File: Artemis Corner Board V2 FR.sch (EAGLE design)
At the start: 102 parts, among them IC1 FT232RL, Q1 BSS138, U1 OPA365AIDBVR, U2 ADS1232IPWR, U3 MCP2562, U4 TM4C123GH6PMI, U5 MCP2562, U6 TPS62177, U7 TPS62175, U8 TPS562219, Y1 16MHz, Y2 32.768kHz

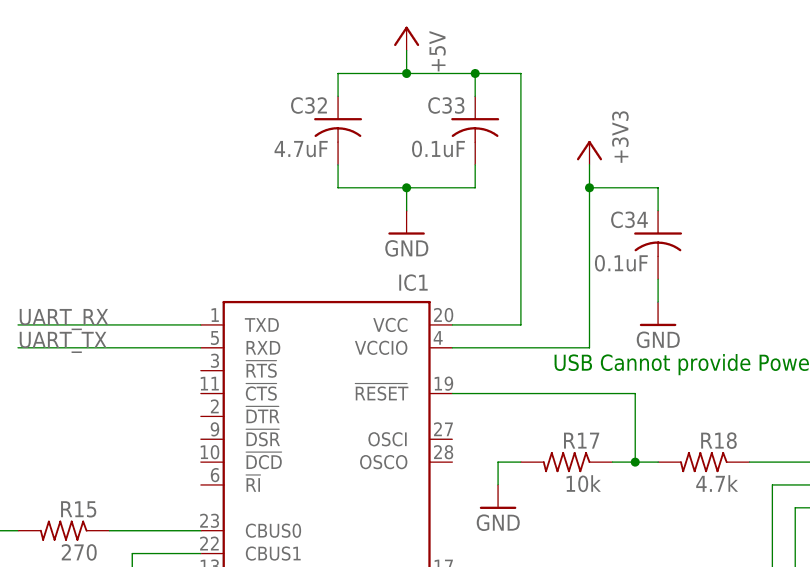
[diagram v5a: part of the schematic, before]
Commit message: Grouped components in layout
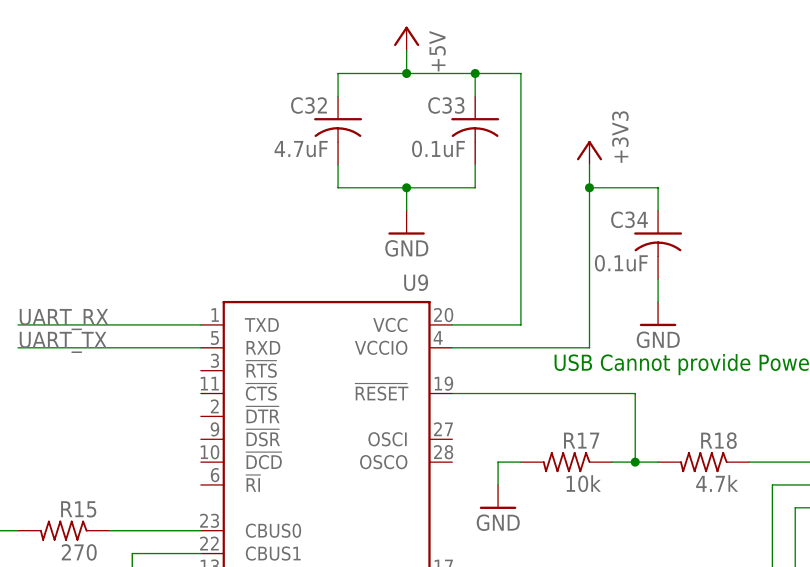
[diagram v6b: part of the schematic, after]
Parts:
- renumbered IC1 to U9
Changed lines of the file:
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@@
 <part name="+3V311" library="supply1" deviceset="+3V3" device=""/>
 <part name="+1V21" library="FormE" deviceset="+1V2" device=""/>
-<part name="IC1" library="ftdichip" deviceset="FT232R" device="L">
+<part name="U9" library="ftdichip" deviceset="FT232R" device="L">
 <attribute name="PARTNO" value="FT232RL-REEL"/>
 </part>
@@
 <instance part="+3V311" gate="G$1" x="878.84" y="185.42"/>
 <instance part="+1V21" gate="G$1" x="878.84" y="124.46"/>
-<instance part="IC1" gate="1" x="612.14" y="200.66" rot="MR0">
+<instance part="U9" gate="1" x="612.14" y="200.66" rot="MR0">
 <attribute name="PARTNO" x="612.14" y="200.66" size="1.778" layer="96" rot="MR0" display="off"/>
 </instance>
@@
 <pinref part="GND37" gate="1" pin="GND"/>
 <wire x1="594.36" y1="170.18" x2="594.36" y2="175.26" width="0.1524" layer="91"/>
-<pinref part="IC1" gate="1" pin="GND@2"/>
+<pinref part="U9" gate="1" pin="GND@2"/>
 <wire x1="594.36" y1="175.26" x2="596.9" y2="175.26" width="0.1524" layer="91"/>
 <wire x1="594.36" y1="175.26" x2="594.36" y2="177.8" width="0.1524" layer="91"/>
 <junction x="594.36" y="175.26"/>
-<pinref part="IC1" gate="1" pin="GND@1"/>
+<pinref part="U9" gate="1" pin="GND@1"/>
 <wire x1="594.36" y1="177.8" x2="596.9" y2="177.8" width="0.1524" layer="91"/>
-<pinref part="IC1" gate="1" pin="GND"/>
+<pinref part="U9" gate="1" pin="GND"/>
 <wire x1="596.9" y1="180.34" x2="594.36" y2="180.34" width="0.1524" layer="91"/>
 <wire x1="594.36" y1="180.34" x2="594.36" y2="177.8" width="0.1524" layer="91"/>
@@
 <wire x1="594.36" y1="180.34" x2="594.36" y2="185.42" width="0.1524" layer="91"/>
 <junction x="594.36" y="180.34"/>
-<pinref part="IC1" gate="1" pin="TEST"/>
+<pinref part="U9" gate="1" pin="TEST"/>
 <wire x1="594.36" y1="185.42" x2="596.9" y2="185.42" width="0.1524" layer="91"/>
 </segment>
 <segment>
 <pinref part="GND40" gate="1" pin="GND"/>
-<pinref part="IC1" gate="1" pin="GND@A"/>
+<pinref part="U9" gate="1" pin="GND@A"/>
 <wire x1="629.92" y1="165.1" x2="629.92" y2="182.88" width="0.1524" layer="91"/>
 <wire x1="629.92" y1="182.88" x2="624.84" y2="182.88" width="0.1524" layer="91"/>
@@
 <wire x1="619.76" y1="254" x2="619.76" y2="251.46" width="0.1524" layer="91"/>
 <junction x="619.76" y="251.46"/>
-<pinref part="IC1" gate="1" pin="VCC"/>
+<pinref part="U9" gate="1" pin="VCC"/>
 <wire x1="624.84" y1="223.52" x2="632.46" y2="223.52" width="0.1524" layer="91"/>
 <wire x1="632.46" y1="223.52" x2="632.46" y2="251.46" width="0.1524" layer="91"/>
@@
 <pinref part="+3V310" gate="G$1" pin="+3V3"/>
 <wire x1="640.08" y1="220.98" x2="640.08" y2="238.76" width="0.1524" layer="91"/>
-<pinref part="IC1" gate="1" pin="VCCIO"/>
+<pinref part="U9" gate="1" pin="VCCIO"/>
 <wire x1="640.08" y1="238.76" x2="640.08" y2="241.3" width="0.1524" layer="91"/>
 <wire x1="624.84" y1="220.98" x2="640.08" y2="220.98" width="0.1524" layer="91"/>
@@
 <segment>
 <label x="576.58" y="220.98" size="1.778" layer="95"/>
-<pinref part="IC1" gate="1" pin="RXD"/>
+<pinref part="U9" gate="1" pin="RXD"/>
 <wire x1="576.58" y1="220.98" x2="596.9" y2="220.98" width="0.1524" layer="91"/>
 </segment>
@@
 <net name="UART_RX" class="0">
 <segment>
-<pinref part="IC1" gate="1" pin="TXD"/>
+<pinref part="U9" gate="1" pin="TXD"/>
 <wire x1="596.9" y1="223.52" x2="576.58" y2="223.52" width="0.1524" layer="91"/>
 <label x="576.58" y="223.52" size="1.778" layer="95"/>
@@
 <wire x1="589.28" y1="198.12" x2="589.28" y2="190.5" width="0.1524" layer="91"/>
 <wire x1="589.28" y1="190.5" x2="586.74" y2="190.5" width="0.1524" layer="91"/>
-<pinref part="IC1" gate="1" pin="CBUS1"/>
+<pinref part="U9" gate="1" pin="CBUS1"/>
 <wire x1="596.9" y1="198.12" x2="589.28" y2="198.12" width="0.1524" layer="91"/>
 </segment>
@@
 <segment>
 <pinref part="R15" gate="G$1" pin="1"/>
-<pinref part="IC1" gate="1" pin="CBUS0"/>
+<pinref part="U9" gate="1" pin="CBUS0"/>
 <wire x1="586.74" y1="200.66" x2="596.9" y2="200.66" width="0.1524" layer="91"/>
 </segment>
@@
 <net name="USB_D_N" class="1">
 <segment>
-<pinref part="IC1" gate="1" pin="USBDM"/>
+<pinref part="U9" gate="1" pin="USBDM"/>
 <wire x1="624.84" y1="187.96" x2="660.4" y2="187.96" width="0.1524" layer="91"/>
 <wire x1="660.4" y1="187.96" x2="660.4" y2="205.74" width="0.1524" layer="91"/>
@@
 <wire x1="670.56" y1="203.2" x2="662.94" y2="203.2" width="0.1524" layer="91"/>
 <wire x1="662.94" y1="203.2" x2="662.94" y2="190.5" width="0.1524" layer="91"/>
-<pinref part="IC1" gate="1" pin="USBDP"/>
+<pinref part="U9" gate="1" pin="USBDP"/>
 <wire x1="662.94" y1="190.5" x2="624.84" y2="190.5" width="0.1524" layer="91"/>
 </segment>
@@
 <pinref part="C35" gate="G$1" pin="1"/>
 <wire x1="652.78" y1="182.88" x2="652.78" y2="195.58" width="0.1524" layer="91"/>
-<pinref part="IC1" gate="1" pin="3V3OUT"/>
+<pinref part="U9" gate="1" pin="3V3OUT"/>
 <wire x1="652.78" y1="195.58" x2="624.84" y2="195.58" width="0.1524" layer="91"/>
 </segment>
@@
 <wire x1="645.16" y1="208.28" x2="645.16" y2="215.9" width="0.1524" layer="91"/>
 <junction x="645.16" y="208.28"/>
-<pinref part="IC1" gate="1" pin="!RESET"/>
+<pinref part="U9" gate="1" pin="!RESET"/>
 <wire x1="645.16" y1="215.9" x2="624.84" y2="215.9" width="0.1524" layer="91"/>
 </segment>

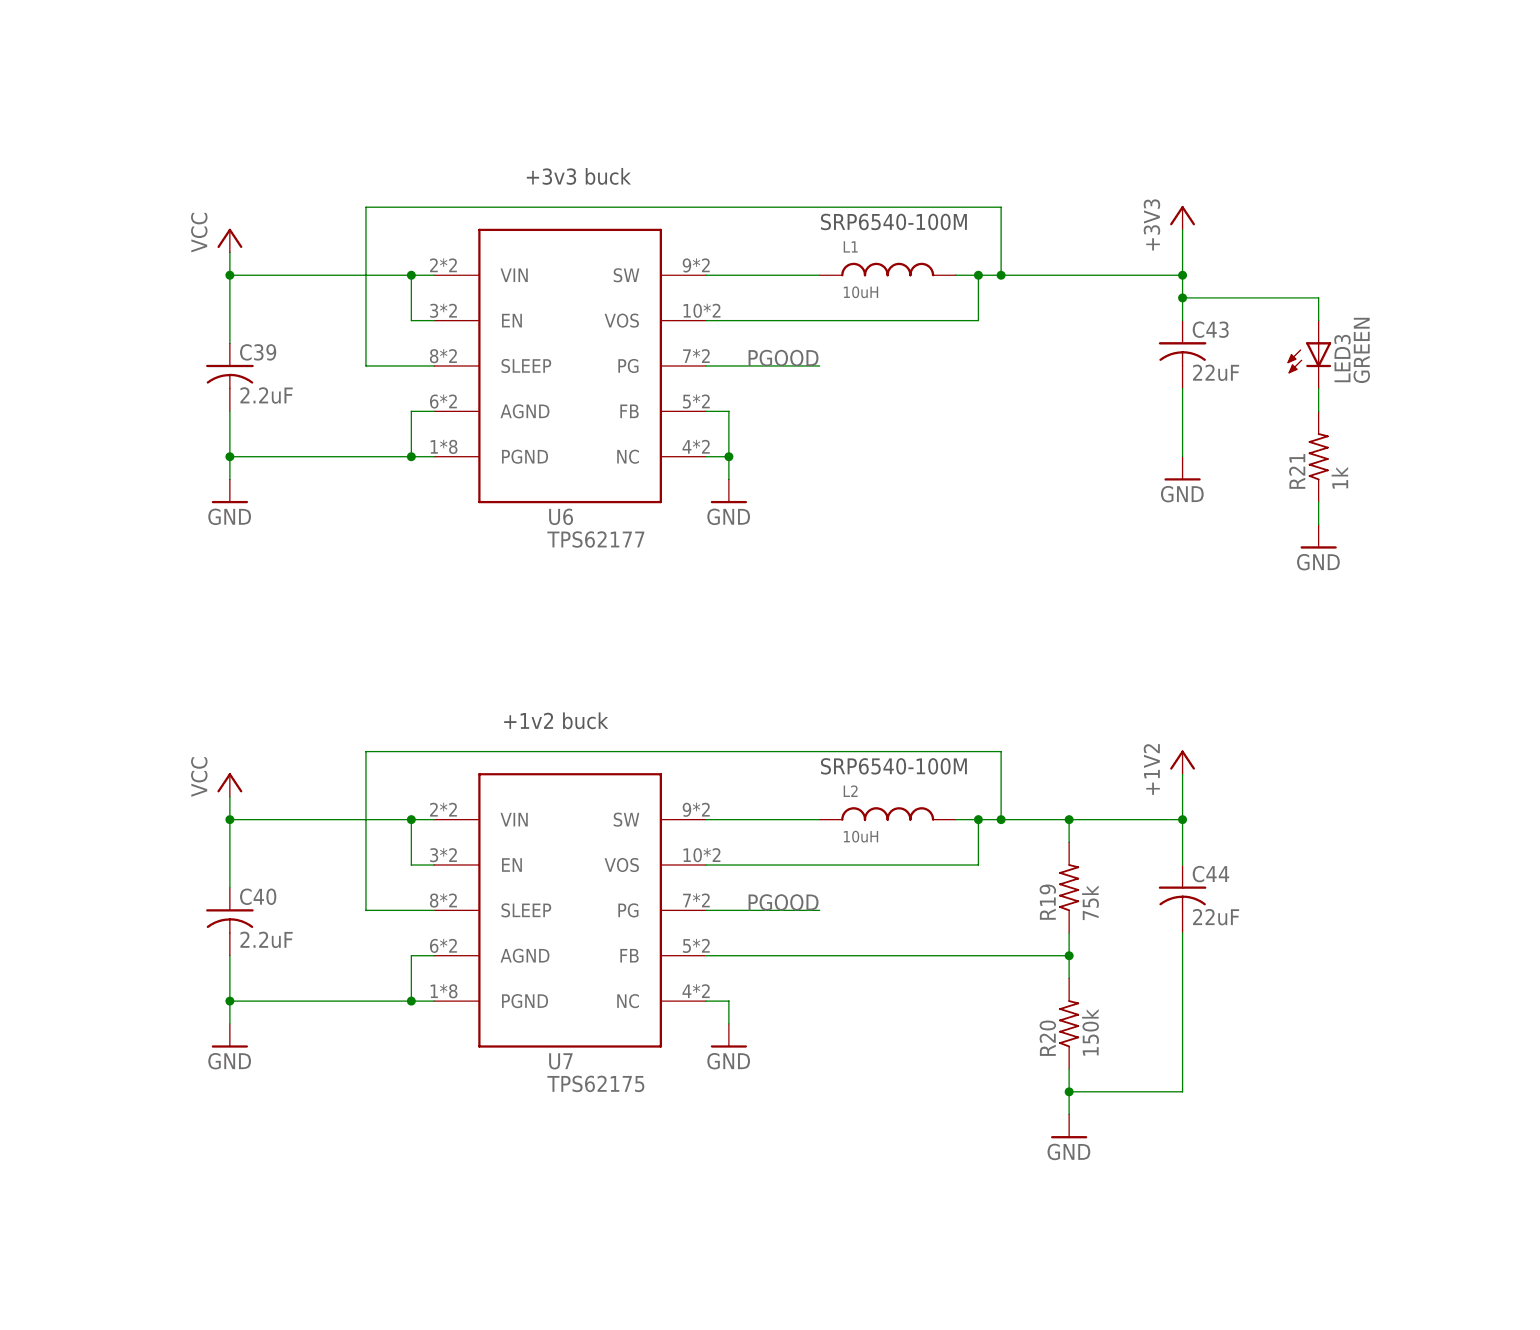
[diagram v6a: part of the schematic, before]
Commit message: Changed to smaller LM3671 regulators
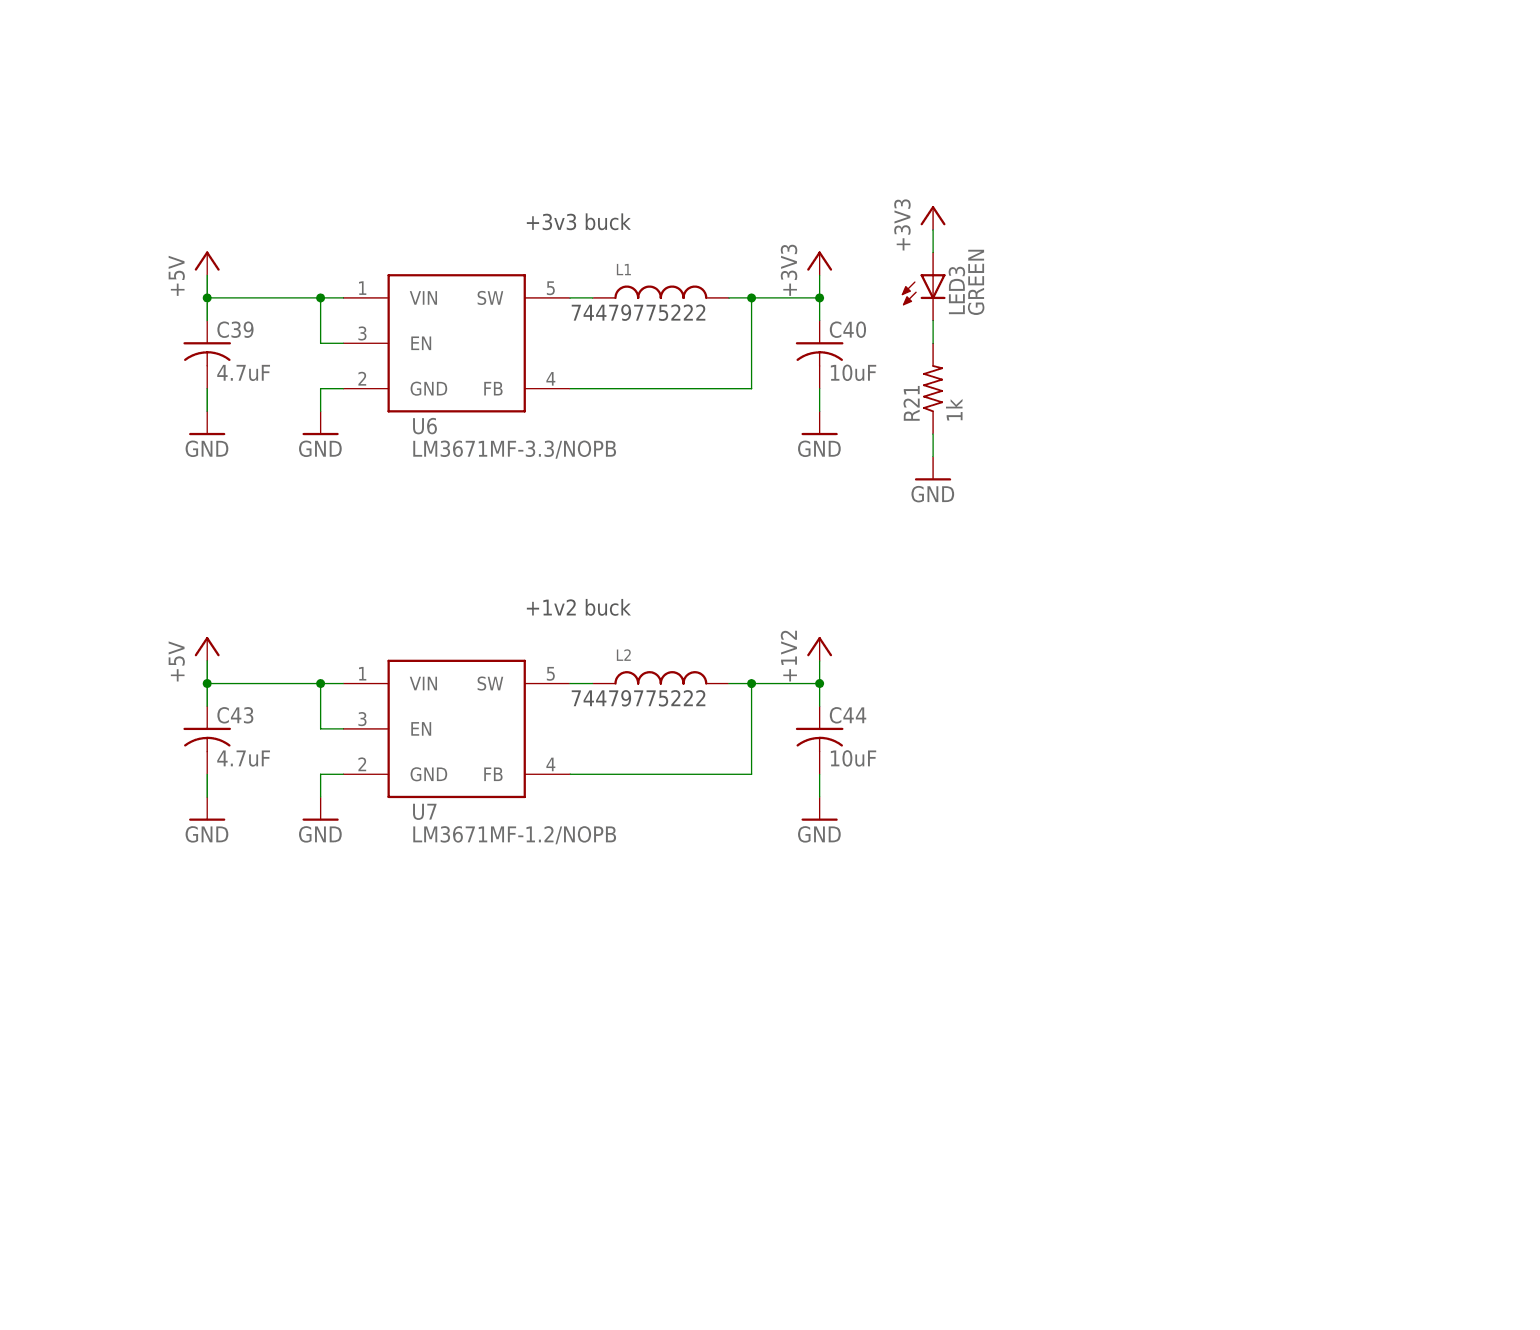
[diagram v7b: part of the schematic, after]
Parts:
- removed R19: 75k, rcl:R-US_R0805
- removed R20: 150k, rcl:R-US_R0805
- C39: value 2.2uF -> 4.7uF; PARTNO UMK212BB7225KG-T -> (none)
- C40: value 2.2uF -> 10uF; PARTNO UMK212BB7225KG-T -> (none)
- C43: value 22uF -> 4.7uF; device rcl:C-USC1210K -> rcl:C-USC0805; PARTNO GRM32ER61E226KE15L -> (none)
- C44: value 22uF -> 10uF; device rcl:C-USC1210K -> rcl:C-USC0805; PARTNO GRM32ER61E226KE15L -> (none)
- L1, L2: value 10uH -> (none); device FormE:SRP6540 -> FormE:L0805; PARTNO SRP6540-100M -> 74479775222
- U6: value TPS62177 -> LM3671MF-3.3/NOPB; device FormE:TPS6217X -> FormE:LM3671MF; PARTNO TPS62177DQCR -> (none)
- U7: value TPS62175 -> LM3671MF-1.2/NOPB; device FormE:TPS6217X -> FormE:LM3671MF; PARTNO TPS62175DQCR -> (none)
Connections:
- net SW_1V2 renamed N$25
- net SW_3V3 renamed N$11
- removed net FB_1V2: R19.1, R20.2, U7.FB
- net +1V2: now also U7.FB; no longer R19.2, U7.SLEEP, U7.VOS
- net +3V3: now also C40.1, U6.FB; no longer C43.1, U6.SLEEP, U6.VOS
- net +5V: now also C39.1, C43.1, U6.EN, U6.VIN, U7.EN, U7.VIN
- net GND: now also U6.GND, U7.GND; no longer R20.1, U6.AGND, U6.FB, U6.NC, U6.PGND, U7.AGND, U7.NC, U7.PGND
- net PGOOD: no longer U6.PG, U7.PG
- net VCC: no longer C39.1, C40.1, U6.EN, U6.VIN, U7.EN, U7.VIN
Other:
- note added: "74479775222"
- note removed: "SRP6540-100M"
- moved on the sheet: C39, C40, C43, C44, L1, L2, LED3, R21

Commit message: Playing with layout arrangement
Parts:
- removed C43: 4.7uF, rcl:C-USC0805
- removed C44: 10uF, rcl:C-USC0805
- removed D1, D2: TPD1E05U06, FormE:TPD1E05U06
- removed L2: (no value), FormE:L0805
- removed R3, R4: 22, rcl:R-US_R0805
- removed U7: LM3671MF-1.2/NOPB, FormE:LM3671MF
- added H3: 1-776231-1, FormE:1-776231-1
- H1: value 1-776231-1 -> 776228-4; device FormE:1-776231-1 -> FormE:776228-4
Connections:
- net N$6 renamed VDDC
- removed net +1V2: C44.1, L2.P$2, U7.FB
- removed net N$20: R3.2, R5.1, U1.NONINVERTING
- removed net N$21: Q1.D, R4.2, R6.1
- removed net N$25: L2.P$1, U7.SW
- net +5V: no longer C43.1, U7.EN, U7.VIN
- net ADC_GAIN_BIT_0: now also U4IO.PD2/AIN5/M0FAULT0/SSI1RX/SSI3RX/USB0EPEN/WT3CCP0; no longer U4IO.PB4/AIN10/CAN0RX/M0PWM2/SSI2CLK/T1CCP0
- net ADC_GAIN_BIT_1: now also U4IO.PD3/AIN4/IDX0/SSI1TX/SSI3TX/USB0PFLT/WT2CCP1; no longer U4IO.PB5/AIN11/CAN0TX/M0PWM3/SSI2FSS/T1CCP1
- net CAR_CAN_N: no longer H1.35
- net CAR_CAN_P: no longer H1.34
- net CAR_CAN_RX: now also U4IO.PF0/C0O/CAN0RX/M1PWM4/NMI/PHA0/SSI1RX/T0CCP0/U1RTS; no longer U4IO.PE4/AIN9/CAN0RX/I2C2SCL/M0PWM4/M1PWM2/U5RX
- net CAR_CAN_TX: now also U4IO.PF3/CAN0TX/M1PWM7/SSI1FSS/T1CCP1/TRCLK; no longer U4IO.PE5/AIN8/CAN0TX/I2C2SDA/M0PWM5/M1PWM3/U5TX
- net DAMPER_POSITION: now also R5.1, U1.NONINVERTING; no longer D1.I/O, H1.25, R3.1
- net GND: no longer C43.2, C44.2, D1.P$2, D2.P$2, U7.GND
- net IR_SENSOR_CAN_N: no longer H1.12
- net IR_SENSOR_CAN_P: no longer H1.11
- net N$15: now also Y2.P$1; no longer Y2.P$3
- net N$17: now also Y2.P$3; no longer Y2.P$1
- net STRAIN_GAUGE_NEGATIVE: no longer H1.26
- net STRAIN_GAUGE_POSITIVE: no longer H1.28
- net WHEEL_TACHOMETER: now also Q1.D, R6.1; no longer D2.I/O, H1.24, R4.1
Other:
- note added: "Wheel Tach 5V"
- note added: "Wheel Tach GND"
- note removed: "+1v2 buck"
- note removed: "Wheel Speed 5V"
- note removed: "Wheel Speed GND"
- moved on the sheet: C30, C31, R14, U5, Y2
